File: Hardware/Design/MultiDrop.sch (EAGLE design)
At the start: 14 parts

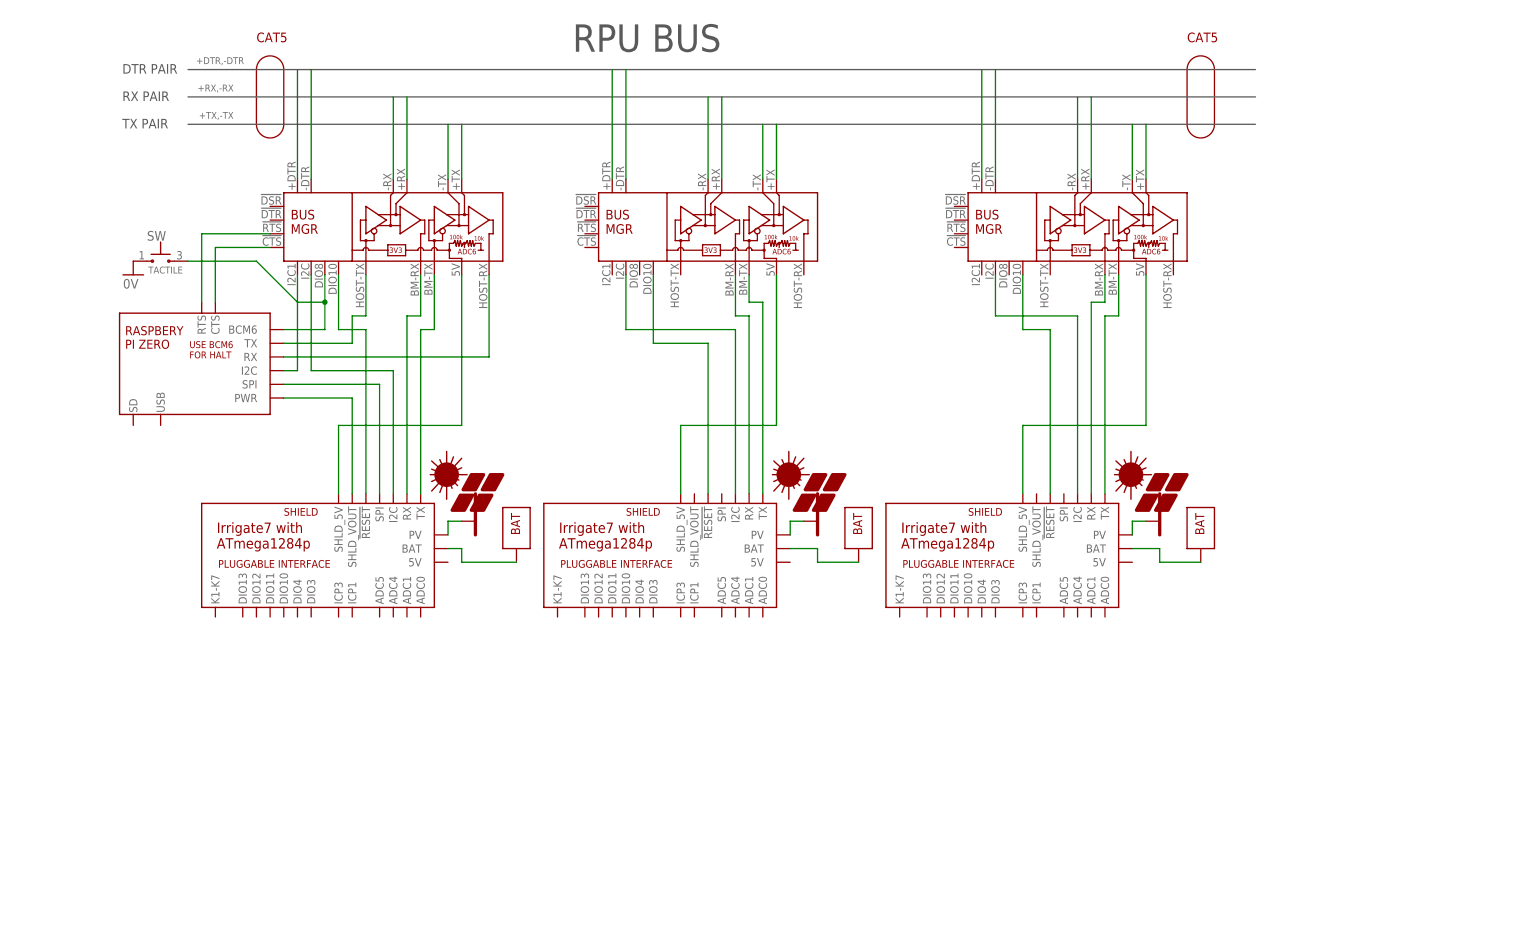
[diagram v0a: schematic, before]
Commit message: Hardware: ^5 reviewing multi-drop example
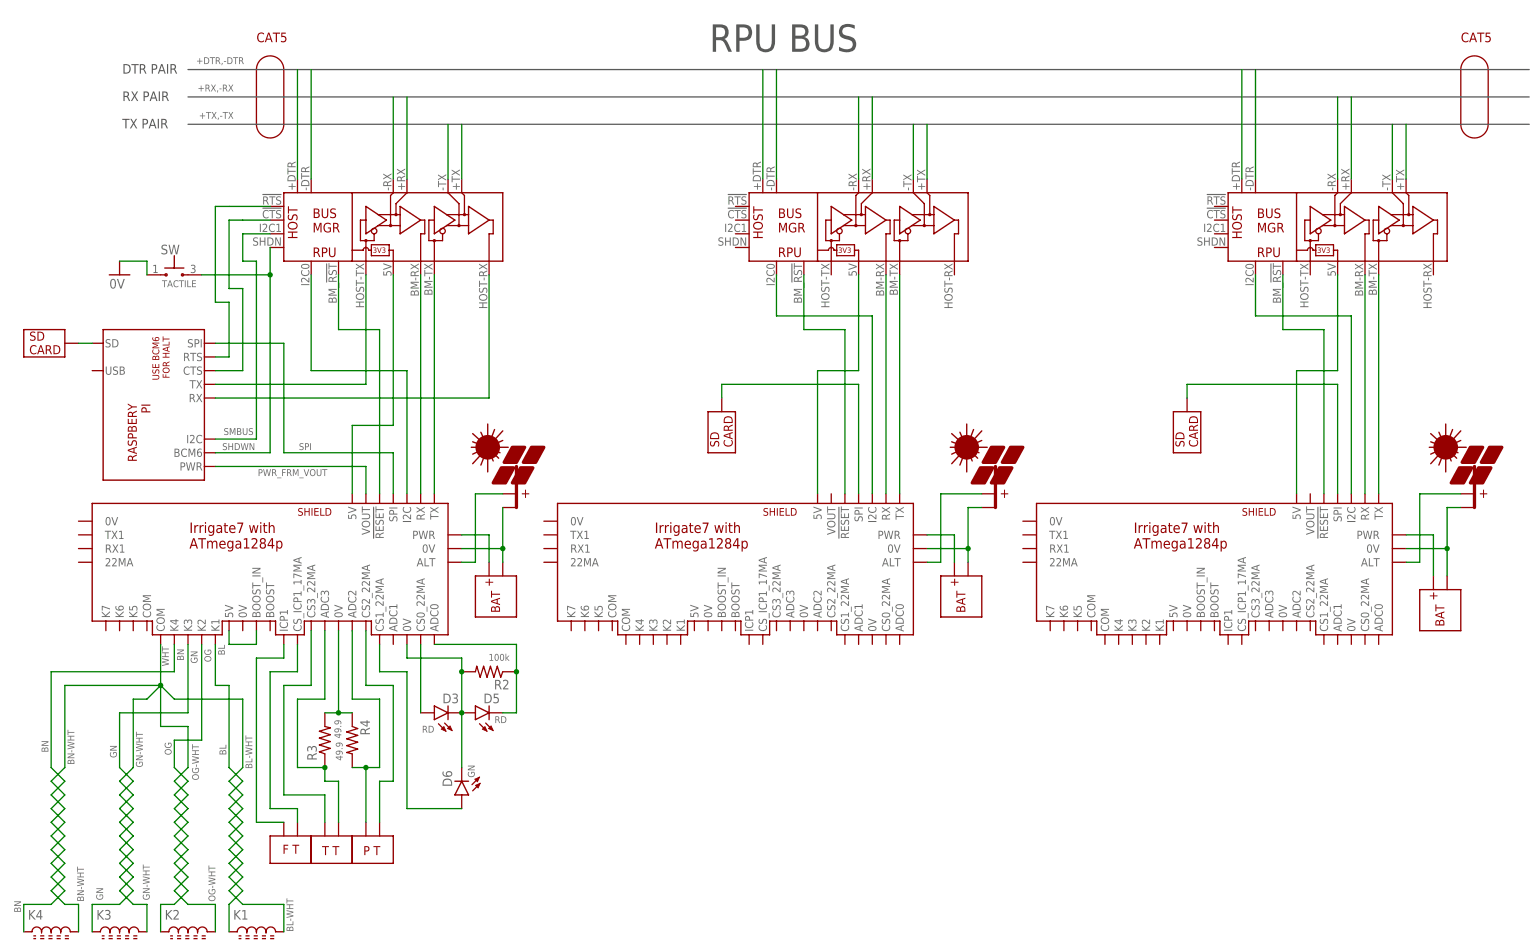
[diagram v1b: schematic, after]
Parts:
- added D3, D5: RD, D-LED:LED5MM
- added D6: GN, D-LED:LED5MM
- added K1, K2, K3, K4: (no value), L-PWR:L0805
- added R2: 100k, R-C:R0805
- added R3, R4: 49.9, R-C:R0805
- added SD1, SD2, SD3: SD, Documentation:SD
- added U$11: PT, Documentation:PT
- added U$12: BUS_MGR, Documentation:BUS_MGR
- added U$13: PI, Documentation:PI
- U$10: value BUS_MGR -> IRRIGATE7; device Documentation:BUS_MGR -> Documentation:IRRIGATE7
- U$3: value PI -> BAT; device Documentation:PI -> Documentation:BAT
- U$4: value BAT -> IRRIGATE7; device Documentation:BAT -> Documentation:IRRIGATE7
- U$5: value BUS_MGR -> FT; device Documentation:BUS_MGR -> Documentation:FT
- U$6: value IRRIGATE7 -> TT; device Documentation:IRRIGATE7 -> Documentation:TT
- U$8: value IRRIGATE7 -> BUS_MGR; device Documentation:IRRIGATE7 -> Documentation:BUS_MGR
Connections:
- removed net N$1 (its old number): U$10.BM_TX, U$8.TX
- removed net N$2 (its old number): U$10.BM_RX, U$8.RX
- removed net N$34: PV4.PV_PWR, U$2.PV
- new net BL: K1.1, U$2.K1
- new net BL-WHT: K1.2
- new net BN: K4.1, U$2.K4
- new net BN-WHT: K4.2
- new net GN: K3.1, U$2.K3
- new net GN-WHT: K3.2
- new net N$14: U$10.TX, U$12.BM_TX
- new net N$16: U$10.PWR, U$7.+BAT
- new net N$18: R3.2, R4.1, U$2.0V@ADC2
- new net N$19: U$2.CS_ICP1_17MA, U$5.PL
- new net N$20: R4.2, U$11.PWR, U$2.ADC2
- new net N$21: U$10.RX, U$12.BM_RX
- new net N$22: PV2.+PV, U$4.ALT
- new net N$23: U$2.5V, U$2.BOOST_IN
- new net N$24: U$2.CS3_22MA, U$6.PWR
- new net N$25: R3.1, U$2.ADC3, U$6.4TO20
- new net N$26: D6.A, U$2.CS1_22MA
- new net N$27: SD3.PV_PWR, U$4.SPI
- new net N$28: SD2.PV_PWR, U$10.SPI
- new net N$37: D5.K, R2.1, U$2.ADC0
- new net N$42: U$4.PWR, U$9.+BAT
- new net N$52: U$2.PWR, U$3.+BAT
- new net N$54: PV1.+PV, U$2.ALT
- new net OG: K2.1, U$2.K2
- new net OG-WHT: K2.2
- new net PWR_FRM_VOUT: U$13.PWR, U$2.VOUT
- new net SHDWN: SW.3, U$1.SHDN, U$13.BCM6
- new net SMBUS: U$1.I2C1, U$13.I2C
- new net SPI: U$13.SPI, U$2.SPI
- new net WHT: U$2.COM@K4
- net +DTR: now also U$1.+DTR; no longer U$10.+DTR
- net +DTR1: now also U$8.+DTR; no longer U$5.+DTR
- net +DTR3: now also U$12.+DTR; no longer U$1.+DTR
- net +RX: now also U$1.+RX; no longer U$10.+RX
- net +RX1: now also U$8.+RX; no longer U$5.+RX
- net +RX3: now also U$12.+RX; no longer U$1.+RX
- net +TX: now also U$1.+TX; no longer U$10.+TX
- net +TX1: now also U$8.+TX; no longer U$5.+TX
- net +TX3: now also U$12.+TX; no longer U$1.+TX
- net -DTR: now also U$1.-DTR; no longer U$10.-DTR
- net -DTR1: now also U$8.-DTR; no longer U$5.-DTR
- net -DTR3: now also U$12.-DTR; no longer U$1.-DTR
- net -RX: now also U$1.-RX; no longer U$10.-RX
- net -RX1: now also U$8.-RX; no longer U$5.-RX
- net -RX3: now also U$12.-RX; no longer U$1.-RX
- net -TX: now also U$1.-TX; no longer U$10.-TX
- net -TX1: now also U$8.-TX; no longer U$5.-TX
- net -TX3: now also U$12.-TX; no longer U$1.-TX
- net N$10: now also U$4.TX, U$8.BM_TX; no longer U$5.BM_TX, U$6.TX
- net N$11: now also U$4.RX, U$8.BM_RX; no longer U$5.BM_RX, U$6.RX
- net N$12: now also PV2.-PV, U$4.0V@PWR, U$9.-BAT; no longer U$4.BAT_PWR, U$8.BAT
- net N$13: now also PV4.-PV, U$10.0V@PWR, U$7.-BAT; no longer SW.3, U$10.DIO8, U$3.BCM6
- net N$15: now also PV4.+PV, U$10.ALT; no longer U$10.I2C1, U$3.I2C
- net N$17: now also U$2.ICP1, U$5.PWR; no longer U$6.BAT, U$9.BAT_PWR
- net N$29: now also U$1.PWR, U$2.5V@SHLD; no longer U$10.PWR, U$8.SHLD_5V
- net N$3: now also SD1.PV_PWR, U$13.SD; no longer U$3.PWR, U$8.SHLD_VOUT
- net N$30: now also U$1.BM-!RST!, U$2.!RESET; no longer U$10.DIO10, U$8.!RESET
- net N$31: now also U$11.4TO20, U$2.CS2_22MA; no longer U$2.BAT, U$7.BAT_PWR
- net N$32: now also U$10.I2C, U$12.I2C0; no longer U$1.I2C, U$2.I2C
- net N$33: now also U$1.I2C0, U$2.I2C; no longer U$10.I2C, U$8.I2C
- net N$36: now also PV1.-PV, U$2.0V@PWR, U$3.-BAT; no longer PV2.PV_PWR, U$6.PV
- net N$4: now also U$1.!CTS, U$13.CTS; no longer U$10.!CTS, U$3.CTS
- net N$41: now also U$10.5V@SHLD, U$12.PWR; no longer U$1.PWR, U$2.SHLD_5V
- net N$43: now also U$10.!RESET, U$12.BM-!RST!; no longer U$1.DIO10, U$2.!RESET
- net N$44: now also U$4.!RESET, U$8.BM-!RST!; no longer U$5.DIO10, U$6.!RESET
- net N$45: now also U$4.5V@SHLD; no longer U$5.PWR, U$6.SHLD_5V
- net N$48: now also U$4.I2C, U$8.I2C0; no longer U$5.I2C, U$6.I2C
- net N$5: now also U$1.!RTS, U$13.RTS; no longer U$10.!RTS, U$3.RTS
- net N$6: now also D3.K, D5.A, D6.K, R2.2, U$2.0V@ADC0; no longer U$3.SPI, U$8.SPI
- net N$7: now also D3.A, U$2.CS0_22MA; no longer PV1.PV_PWR, U$8.PV
- net N$8: now also U$1.HOST_RX, U$13.RX; no longer U$10.HOST_RX, U$3.RX
- net N$9: now also U$1.HOST_TX, U$13.TX; no longer U$10.HOST_TX, U$3.TX
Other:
- note added: "DAY-NIGHT"
- note added: "FLOW"
- note added: "K7"
- note added: "LIGHT SENSOR"
- note added: "STATUS"
- note removed: "20W PV"
- note removed: "3W PV"
- note removed: "50 AHr"
- note removed: "7.5AHr"
- note removed: "USB WiFi USB Ethernet USB OTG"
- moved on the sheet: SW

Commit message: Hardware: ^5 testing, selftest is needed
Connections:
- net SMBUS: now also U$1.SMBUS; no longer U$1.I2C1
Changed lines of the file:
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@@
 <wire x1="43.18" y1="68.58" x2="40.64" y2="68.58" width="0.1524" layer="91"/>
 <wire x1="40.64" y1="68.58" x2="40.64" y2="73.66" width="0.1524" layer="91"/>
-<pinref part="U$1" gate="G$1" pin="I2C1"/>
+<pinref part="U$1" gate="G$1" pin="SMBUS"/>
 <wire x1="40.64" y1="73.66" x2="45.72" y2="73.66" width="0.1524" layer="91"/>
 <label x="37.084" y="36.322" size="1.27" layer="91"/>
